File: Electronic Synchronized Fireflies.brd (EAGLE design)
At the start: 45 x 45 mm, 42 parts, among them Q1 NPN, Q2 DMP2035U-7, U2 MSP430G2231/TSSOP-14, X1 22-23-2021, X2 22-23-2031, X3 22-23-2021

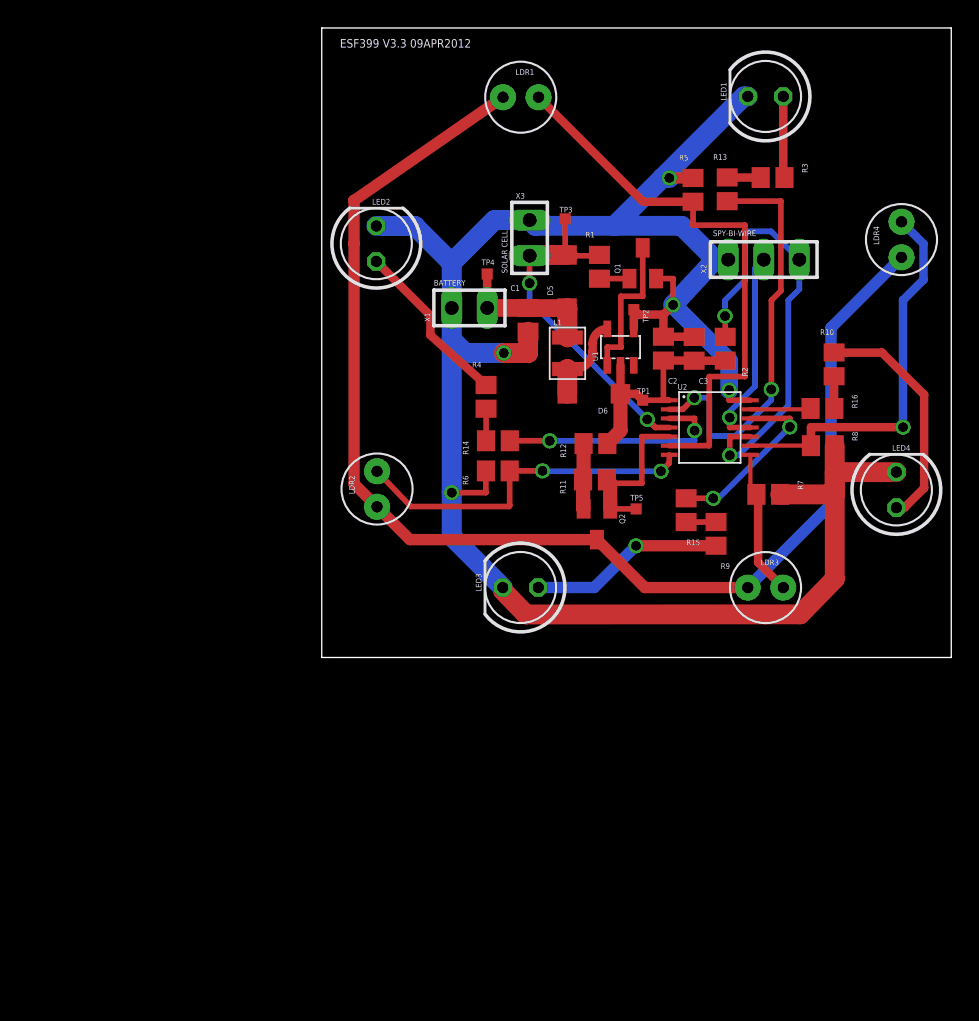
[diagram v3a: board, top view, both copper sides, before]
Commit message: Reduced number of parts, LDRs to phototransistors
v1.1 Changed from 4 pairs of LEDs and LDRs to three pairs of LEDs and
phototransistors. Replaced power transistor with MOSFET and solar cell
connection with surface mount photocell.
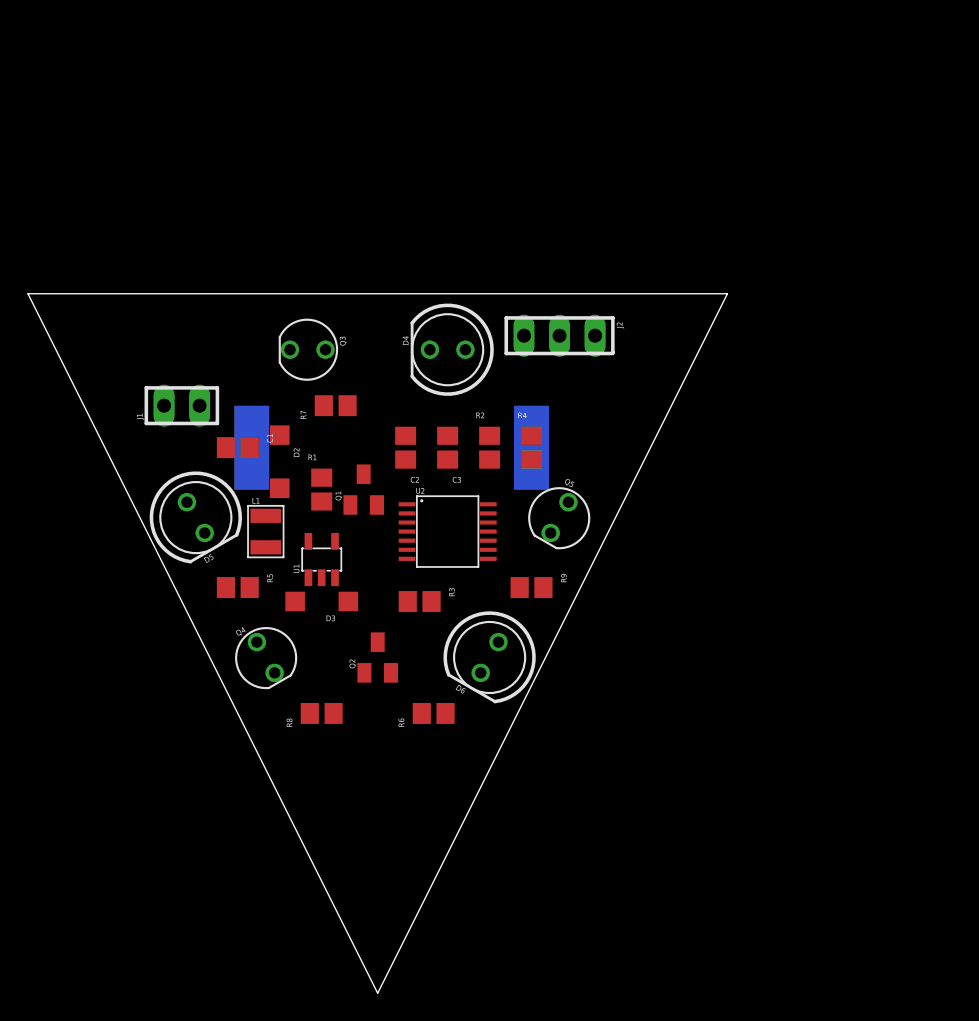
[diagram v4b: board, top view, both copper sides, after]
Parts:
- removed LDR1, LDR2, LDR3, LDR4: LDR, Firefly:LDR5MM
- removed LED1, LED2, LED3, LED4: (no value), Firefly:LED5MM
- removed R10: 56ohm, Firefly:R0805
- removed R11: 20kohm, Firefly:R0805
- removed R12, R13, R14, R15, R16: 0ohm, Firefly:R0805
- removed TP1, TP2, TP3, TP4, TP5: TPTP08SQ, Firefly:TP08SQ
- removed X1, X3: 22-23-2021, Firefly:22-23-2021
- removed X2: 22-23-2031, Firefly:22-23-2031
- added D1: KXOB22-04X3, Electronic Synchronized Fireflies:KXOB22-04X3
- added D2, D3: MBR0520LT, Electronic Synchronized Fireflies:SOD123
- added D4: LED, Electronic Synchronized Fireflies:LED5MM
- added J1: (no value), Electronic Synchronized Fireflies:2WIRE_HEADER
- added J2: (no value), Electronic Synchronized Fireflies:3WIRE_HEADER
- added Q3, Q4, Q5: LPT80A, Electronic Synchronized Fireflies:LPT80A
- C1, C2, C3: device Firefly:C0805 -> Electronic Synchronized Fireflies:CAPACITOR_0805
- D5, D6: value MBR0520LT -> LED; device Firefly:SOD123 -> Electronic Synchronized Fireflies:LED5MM
- L1: device Firefly:INDUCTOR_1007 -> Electronic Synchronized Fireflies:INDUCTOR_1007
- Q1: value NPN -> BSS123; device Firefly:SOT23 -> Electronic Synchronized Fireflies:SOT23
- Q2: value DMP2035U-7 -> BSS84; device Firefly:SOT23 -> Electronic Synchronized Fireflies:SOT23
- R1, R2, R4, R7, R8: device Firefly:R0805 -> Electronic Synchronized Fireflies:RESISTOR_0805
- R3, R9: value 56ohm -> 20kohm; device Firefly:R0805 -> Electronic Synchronized Fireflies:RESISTOR_0805
- R5, R6: value 20kohm -> 56ohm; device Firefly:R0805 -> Electronic Synchronized Fireflies:RESISTOR_0805
- U1: value (none) -> NCP1400A; device Firefly:SOT23-5 -> Electronic Synchronized Fireflies:SOT23-5
- U2: value MSP430G2231/TSSOP-14 -> MSP430G2231; device Firefly:PW14 -> Electronic Synchronized Fireflies:TSSOP-14
- moved R5 43.2 mm to (15.0, 29.0), turned to 180 degrees
- moved R8 40.6 mm to (21.0, 20.0), turned to 0 degrees
- moved R3 39.4 mm to (28.0, 28.0)
- moved R7 31.6 mm to (22.0, 42.0), turned to 0 degrees
- moved D5 31.4 mm to (12.0, 34.0), turned to 300 degrees
- moved U1 26.2 mm to (21.0, 31.0)
- moved Q1 25.7 mm to (24.0, 36.0)
- moved R1 25.4 mm to (21.0, 36.0)
- moved L1 25.0 mm to (17.0, 33.0)
- moved C1 22.7 mm to (15.0, 39.0), turned to 180 degrees
- moved D6 20.3 mm to (33.0, 24.0), turned to 240 degrees
- moved U2 20.2 mm to (30.0, 33.0)
- moved C2 19.7 mm to (27.0, 39.0)
- moved C3 19.0 mm to (30.0, 39.0)
- moved Q2 18.3 mm to (25.0, 24.0), turned to 0 degrees
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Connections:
- removed net N$19: R13.1, R3.2
- removed net N$23: R15.2, U2.12
- removed net N$24: LED1.A, R3.1
- removed net N$25: R10.2, R16.1
- removed net N$26: R15.1, R9.2
- removed net N$29: LDR3.A, R7.2, U2.8
- removed net N$30: LDR4.A, R8.2, U2.9
- removed net N$31: LED3.A, R9.1
- removed net N$32: LED4.A, R10.1
- removed net N$7 (its old number): U1.3
- new net N$2: D1.P$1, D2.A, R1.1, U2.4
- new net N$6: Q1.2, U1.1
- new net N$9: J2.3, R2.2, U2.10
- net GND: now also D1.P$2, D4.K, D5.K, D6.K, J1.1, J2.1, Q1.3, Q3.E, Q4.E, Q5.E; no longer LED1.K, LED2.K, LED3.K, LED4.K, Q1.2, R5.1, R6.1, R7.1, R8.1, TP2.TP, X1.1, X2.1, X3.1
- net N$1: now also C1.1, D2.C, J1.2, L1.P$1; no longer LDR1.K, LDR2.K, LDR3.K, LDR4.K, Q2.3
- net N$10: now also Q2.2, R3.1; no longer Q1.3, U1.1
- net N$11: now also J2.2, U2.11; no longer R13.2, U2.2
- net N$12: now also Q2.3, R7.2, R8.2, R9.2; no longer R14.2, U2.3
- net N$13: now also Q4.C, R8.1, U2.7; no longer D5.A, R1.1, TP3.TP, U2.4, X3.2
- net N$14: now also Q3.C, R7.1, U2.6; no longer R2.2, U2.10, X2.3
- net N$15: now also Q5.C, R9.1, U2.8; no longer Q2.2, R11.1, R12.1
- net N$16: now also R4.2, U2.2; no longer LDR2.A, R6.2, U2.7
- net N$17: now also U2.3; no longer LDR1.A, U2.6
- net N$18: now also R6.2, U2.12; no longer LED2.A, R4.1
- net N$20: now also D5.A, R5.1; no longer U2.11, X2.2
- net N$21: now also D6.A, R6.1; no longer R16.2, U2.13
- net N$22: now also D4.A, R4.1; no longer R14.1, R4.2
- net N$3: now also D3.A, L1.P$2, U1.5; no longer Q2.1, R11.2, TP5.TP, U2.5
- net N$4: now also Q2.1, R3.2, U2.5; no longer C1.1, D5.C, L1.P$1, TP4.TP, X1.2
- net N$5: now also C3.1, D3.C, R2.1, U1.2, U2.1; no longer D6.A, L1.P$2, U1.5
- net N$8: now also U1.3; no longer C3.1, D6.C, R12.2, R2.1, TP1.TP, U1.2, U2.1
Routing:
- net GND: track 151.4 -> 0.00 mm, vias 5 -> 0
- net N$1: track 92.6 -> 0.00 mm
- net N$17: track 40.7 -> 0.00 mm
- net N$14: track 32.1 -> 0.00 mm, vias 2 -> 0
- net N$11: track 29.8 -> 0.00 mm, vias 2 -> 0
- net N$30: track 28.2 -> 0.00 mm, vias 1 -> 0
- net N$16: track 25.3 -> 0.00 mm, vias 2 -> 0
- net N$13: track 24.8 -> 0.00 mm, vias 2 -> 0
- net N$8: track 17.3 -> 0.00 mm
- net N$32: track 16.9 -> 0.00 mm
- net N$12: track 16.6 -> 0.00 mm, vias 2 -> 0
- net N$20: track 14.5 -> 0.00 mm, vias 1 -> 0
- net N$31: track 13.9 -> 0.00 mm, vias 1 -> 0
- net N$23: track 13.0 -> 0.00 mm, vias 2 -> 0
- net N$18: track 12.2 -> 0.00 mm
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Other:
- board size 45 x 45 mm -> 50 x 50 mm
- board text removed: "BATTERY"
- board text removed: "ESF399 V3.3 09APR2012"
- board text removed: "SOLAR CELL"
- board text removed: "SPY-BI-WIRE"

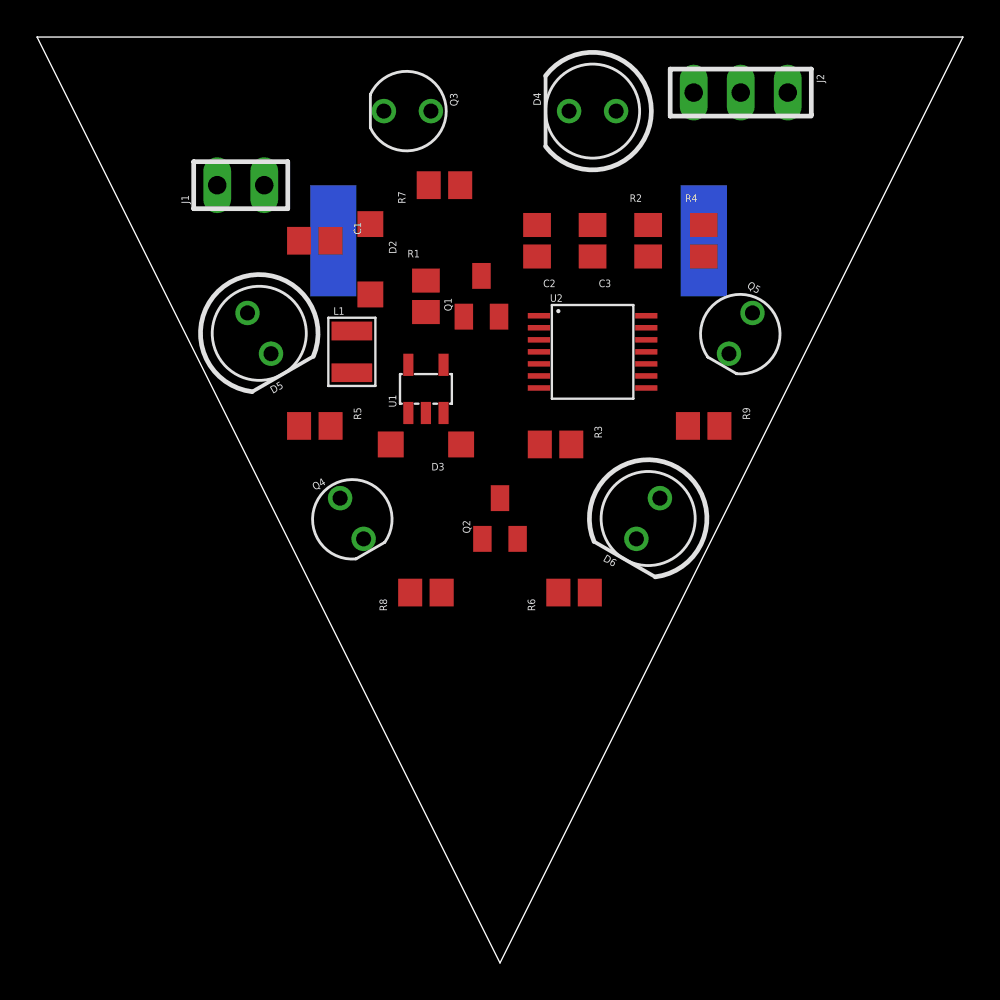
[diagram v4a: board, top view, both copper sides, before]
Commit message: Updated board / schematic / library
Smaller PCB footprint, added frames to board layout.
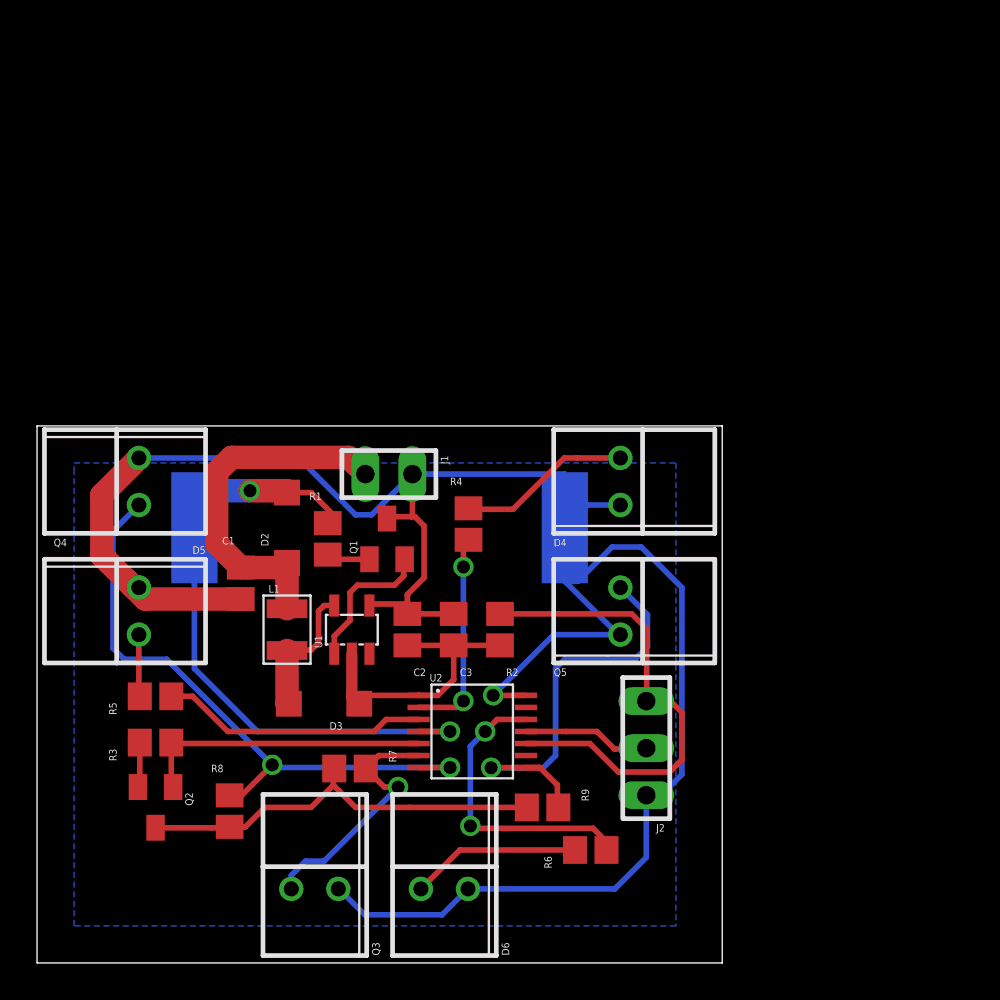
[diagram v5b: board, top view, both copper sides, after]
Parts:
- added FRAME1: (no value), Electronic Synchronized Fireflies:FRAME_A_L
- added U$1: DOCFIELD, Electronic Synchronized Fireflies:DOCFIELD
- D4, D5, D6: device Electronic Synchronized Fireflies:LED5MM -> Electronic Synchronized Fireflies:LED5MMRT
- Q3, Q4, Q5: device Electronic Synchronized Fireflies:LPT80A -> Electronic Synchronized Fireflies:LED5MMRT
- R1, R2, R3, R7, R8, R9: value 20kohm -> 20kR
- R4, R5, R6: value 56ohm -> 56R
- moved Q3 42.3 mm to (15.0, 4.00), turned to 0 degrees
- moved J2 35.8 mm to (32.9, 11.6), turned to 90 degrees
- moved R7 31.9 mm to (16.9, 10.5), turned to 180 degrees
- moved R3 26.9 mm to (6.40, 11.9), turned to 0 degrees
- moved Q2 24.3 mm to (6.40, 8.40), turned to 180 degrees
- moved D6 22.8 mm to (22.0, 4.00), turned to 0 degrees
- moved R2 22.5 mm to (25.0, 18.0), turned to 90 degrees
- moved R9 22.4 mm to (27.3, 8.40)
- moved C3 22.3 mm to (22.5, 18.0)
- moved C2 22.1 mm to (20.0, 18.0)
- moved U2 21.5 mm to (23.5, 12.5)
- moved D4 20.1 mm to (31.5, 26.0), turned to 270 degrees
- moved R4 19.9 mm to (23.3, 23.7)
- moved C1 18.9 mm to (11.0, 20.5), turned to 270 degrees
- moved J1 17.5 mm to (19.0, 26.4), turned to 180 degrees
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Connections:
- removed net N$8: C2.1, U1.3
- net GND: now also Q3.K, Q4.K, Q5.K; no longer Q3.E, Q4.E, Q5.E
- net N$13: now also Q4.A; no longer Q4.C
- net N$14: now also Q3.A; no longer Q3.C
- net N$15: now also Q5.A; no longer Q5.C
- net N$5: now also C2.1
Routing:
- net GND: track 0.00 -> 119.0 mm, vias 0 -> 1
- net N$2: track 0.00 -> 35.1 mm, vias 0 -> 2
- net N$13: track 0.00 -> 34.2 mm, vias 0 -> 2
- net N$9: track 0.00 -> 26.2 mm
- net N$15: track 0.00 -> 23.7 mm, vias 0 -> 1
- net N$12: track 0.00 -> 22.4 mm
- net N$1: track 0.00 -> 19.6 mm
- net N$18: track 0.00 -> 16.1 mm, vias 0 -> 2
- net N$4: track 0.00 -> 15.8 mm
- net N$5: track 0.00 -> 15.4 mm
- net N$17: track 0.00 -> 14.4 mm
- net N$14: track 0.00 -> 13.8 mm, vias 0 -> 1
- net N$16: track 0.00 -> 11.4 mm, vias 0 -> 2
- net N$22: track 0.00 -> 9.37 mm
- net N$21: track 0.00 -> 9.19 mm
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- added copper zone on layer 16, net GND
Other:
- board size 50 x 50 mm -> 37 x 29 mm
